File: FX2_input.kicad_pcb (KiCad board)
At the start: 2 copper layers, 53.3 x 43.2 mm, 38 parts, among them P1 CONN_10X2, P2 CONN_10X2, P3 CONN_9, P4 CONN_9

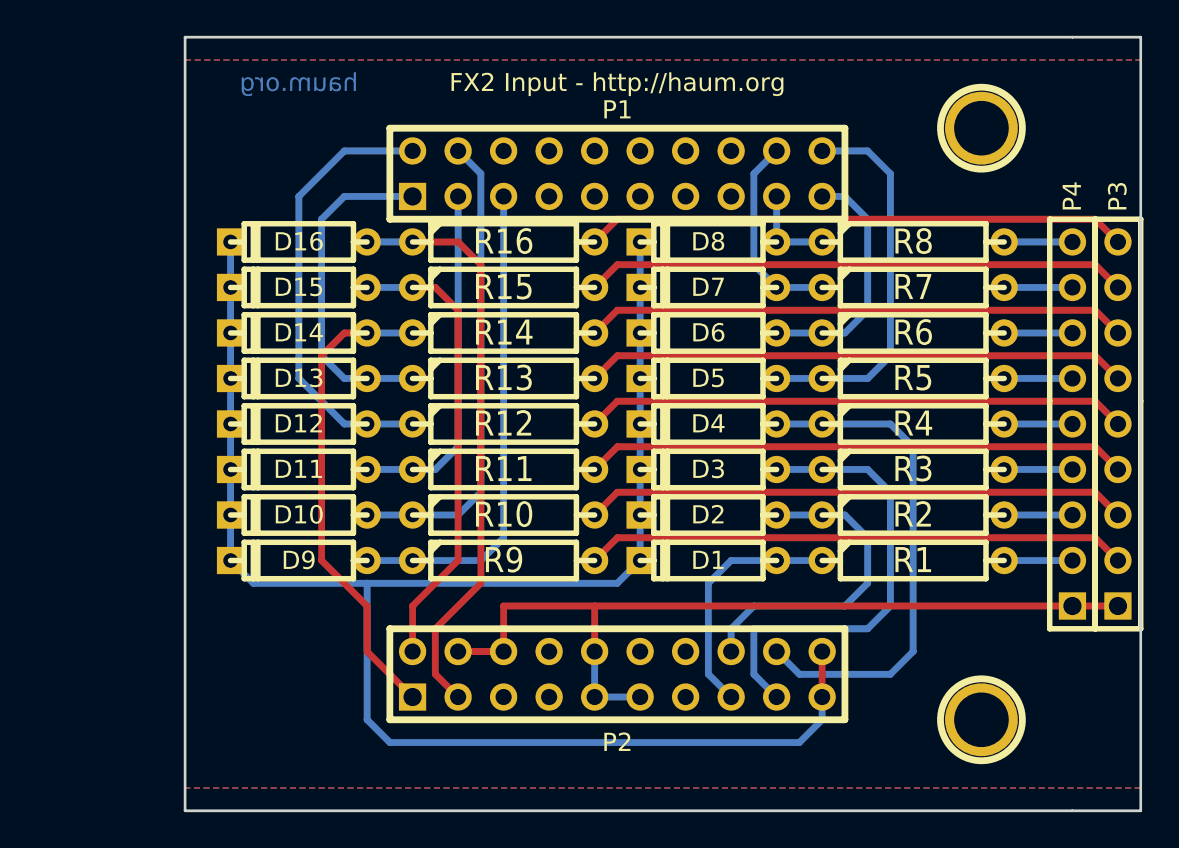
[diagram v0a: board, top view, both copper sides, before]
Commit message: redessin carte et positionnement fixation - inter (WIP)
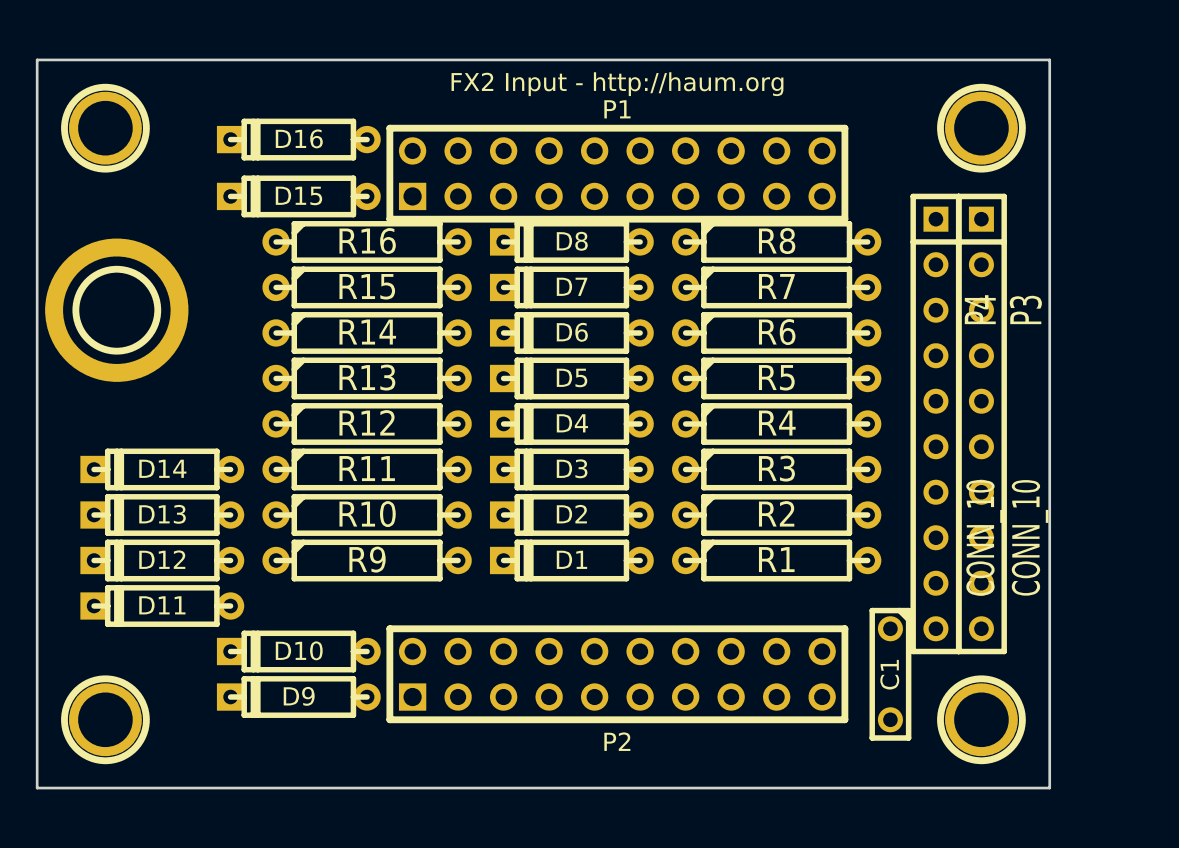
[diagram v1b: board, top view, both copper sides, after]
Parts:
- added 1PIN: P***, 1pin, F.Cu at (140.3, 132.1)
- added 1PIN: P***, 1pin, F.Cu at (140.3, 99.1)
- added 1PIN: P***, 1pin, F.Cu at (141.0, 109.2)
- added C1: 100nF, C2, F.Cu at (184.2, 129.5)
- P3, P4: value CONN_9 -> CONN_10; footprint PIN_ARRAY_9x1 -> SIL-10
- moved D11 10.8 mm to (143.5, 125.7)
- moved D12 10.8 mm to (143.5, 123.2)
- moved D13 10.8 mm to (143.5, 120.7)
- moved D14 10.8 mm to (143.5, 118.1)
- moved D1 7.62 mm to (166.4, 123.2)
- moved D10 7.62 mm to (151.1, 128.3)
- moved D2 7.62 mm to (166.4, 120.7)
- moved D3 7.62 mm to (166.4, 118.1)
- moved D4 7.62 mm to (166.4, 115.6)
- moved D5 7.62 mm to (166.4, 113.0)
- moved D6 7.62 mm to (166.4, 110.5)
- moved D7 7.62 mm to (166.4, 108.0)
- moved D8 7.62 mm to (166.4, 105.4)
- moved D9 7.62 mm to (151.1, 130.8)
- moved P3 7.62 mm to (189.2, 115.6), turned to 270 degrees
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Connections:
- P2 pad 10: /GND -> GND
- P2 pad 11: /GND -> GND
- P2 pad 4: /GND -> GND
- P2 pad 6: /GND -> GND
- P2 pad 9: /GND -> GND
- P3 pad 1: /GND -> N-0000025
- P3 pad 2: N-0000049 -> N-0000052
- P3 pad 3: N-0000051 -> N-0000023
- P3 pad 4: N-0000050 -> N-0000022
- P3 pad 5: N-0000019 -> N-0000021
- P3 pad 6: N-0000018 -> N-0000053
- P3 pad 7: N-0000017 -> N-0000020
- P3 pad 8: N-0000011 -> N-0000019
- P3 pad 9: N-0000015 -> N-0000049
- P4 pad 1: /GND -> N-0000024
- P4 pad 2: N-0000020 -> N-0000050
- P4 pad 3: N-0000023 -> N-0000038
- P4 pad 4: N-0000024 -> N-0000037
- P4 pad 5: N-0000025 -> N-0000048
- P4 pad 6: N-0000016 -> N-0000036
- P4 pad 7: N-0000012 -> N-0000051
- P4 pad 9: N-0000014 -> N-0000012
- R1 pad 2: N-0000020 -> N-0000012
- R10 pad 2: N-0000051 -> N-0000019
- R11 pad 2: N-0000050 -> N-0000020
- R12 pad 2: N-0000019 -> N-0000053
- R13 pad 2: N-0000018 -> N-0000021
- R14 pad 2: N-0000017 -> N-0000022
- R15 pad 2: N-0000011 -> N-0000023
- R16 pad 2: N-0000015 -> N-0000052
- R2 pad 2: N-0000023 -> N-0000013
- R3 pad 2: N-0000024 -> N-0000051
- R4 pad 2: N-0000025 -> N-0000036
- R5 pad 2: N-0000016 -> N-0000048
- R6 pad 2: N-0000012 -> N-0000037
- R7 pad 2: N-0000013 -> N-0000038
- R8 pad 2: N-0000014 -> N-0000050
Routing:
- net /3.3v: track 97.4 -> 0.00 mm
- net /GND: track 47.0 -> 0.00 mm
- net /PD7: track 32.6 -> 0.00 mm
- net N-0000051: track 30.3 -> 0.00 mm
- net N-0000050: track 30.3 -> 0.00 mm
- net N-0000049: track 30.3 -> 0.00 mm
- net N-0000019: track 30.3 -> 0.00 mm
- net N-0000018: track 30.3 -> 0.00 mm
- net N-0000017: track 30.3 -> 0.00 mm
- net N-0000015: track 30.3 -> 0.00 mm
- net N-0000011: track 30.3 -> 0.00 mm
- net /PB3: track 28.2 -> 0.00 mm
- net /PD0: track 27.2 -> 0.00 mm
- net /PD5: track 26.8 -> 0.00 mm
- net /PD1: track 26.5 -> 0.00 mm
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- removed copper zone on B.Cu, net /GND
- removed copper zone on F.Cu, net /GND
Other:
- board size 53.3 x 43.2 mm -> 56.5 x 40.6 mm
- board text removed: "haum.org"

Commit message: new version - fit base board & power on connector
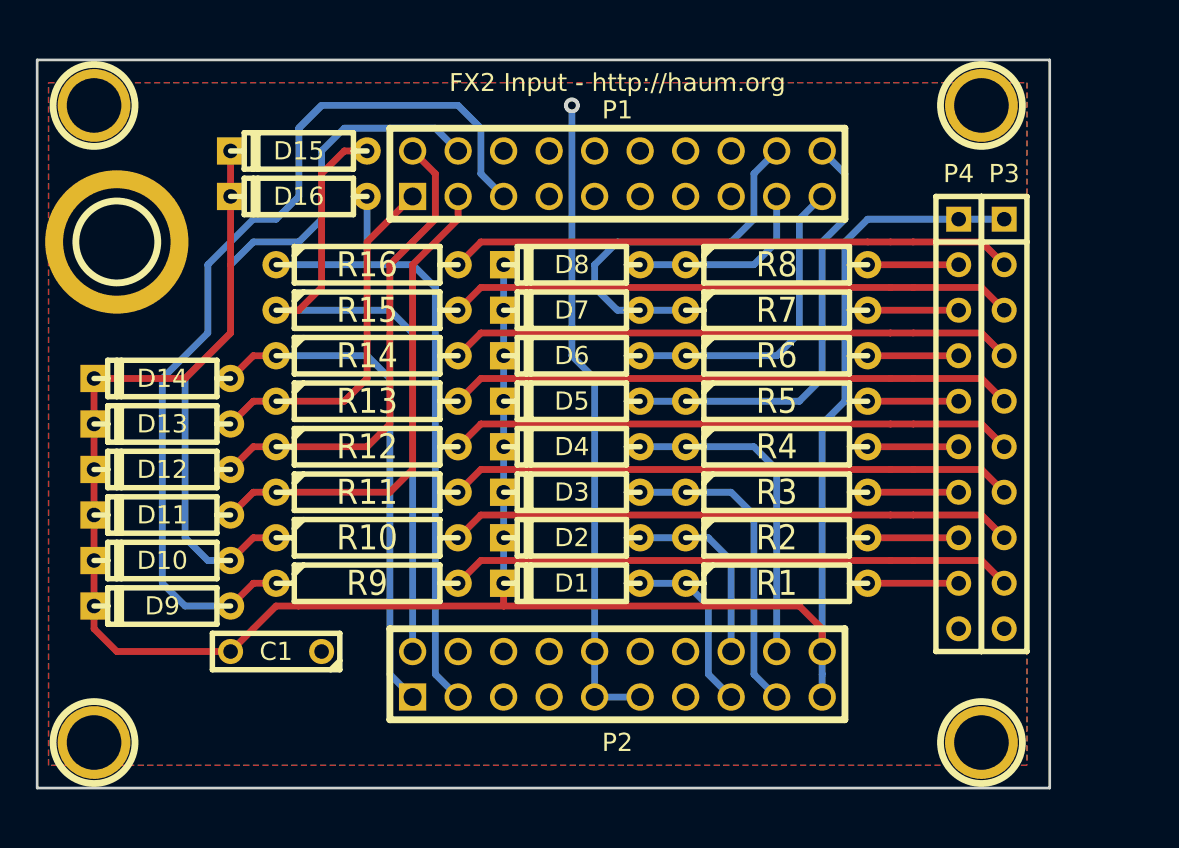
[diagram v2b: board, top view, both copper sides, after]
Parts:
- moved C1 34.3 mm to (149.9, 128.3), turned to 180 degrees
- moved D10 9.16 mm to (143.5, 123.2)
- moved D9 9.16 mm to (143.5, 125.7)
- moved D13 5.08 mm to (143.5, 115.6)
- moved D11 5.08 mm to (143.5, 120.7)
- moved D12 5.08 mm to (143.5, 118.1)
- moved D14 5.08 mm to (143.5, 113.0)
- moved 1PIN 3.81 mm to (141.0, 105.4)
- moved D16 3.18 mm to (151.1, 102.9)
- moved D15 2.54 mm to (151.1, 100.3)
- moved 1PIN 1.42 mm to (139.7, 97.8)
- moved 1PIN 1.42 mm to (139.7, 133.3)
- moved D4 1.27 mm to (166.4, 116.8)
- moved D6 1.27 mm to (166.4, 111.8)
- moved D8 1.27 mm to (166.4, 106.7)
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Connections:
- P3 pad 1: N-0000025 (its old number) -> /3.3v
- P4 pad 1: N-0000024 (its old number) -> /3.3v
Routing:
- net /3.3v: track 0.00 -> 131.2 mm
- net /PD0: track 0.00 -> 54.0 mm
- net /PD1: track 0.00 -> 41.0 mm
- net /PD6: track 0.00 -> 38.4 mm
- net /PD7: track 0.00 -> 36.6 mm
- net GND: track 0.00 -> 36.1 mm, vias 0 -> 1
- net N-0000050: track 0.00 -> 31.5 mm
- net N-0000049: track 0.00 -> 31.5 mm
- net N-0000021: track 0.00 -> 31.5 mm
- net N-0000051: track 0.00 -> 31.5 mm
- net N-0000044: track 0.00 -> 31.5 mm
- net N-0000022: track 0.00 -> 31.5 mm
- net N-0000020: track 0.00 -> 31.5 mm
- net N-0000018: track 0.00 -> 31.5 mm
- net /PD5: track 0.00 -> 28.2 mm
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- added copper zone on B.Cu, net GND
- added copper zone on F.Cu, net GND
